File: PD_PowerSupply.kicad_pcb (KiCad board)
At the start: 2 copper layers, 77.1 x 77.1 mm, 12 parts, among them Q1 STL6P3LLH6, Q2 STL6P3LLH6, Q3 MMBT3906, Q4 MMBT3906, U1 STUSB4500QTR, U2 ESP32-WROOM-32, U3 CP2102N, U4 LTM8074IY#PBF, U5 LTM8074IY#PBF, U6 LTC2972

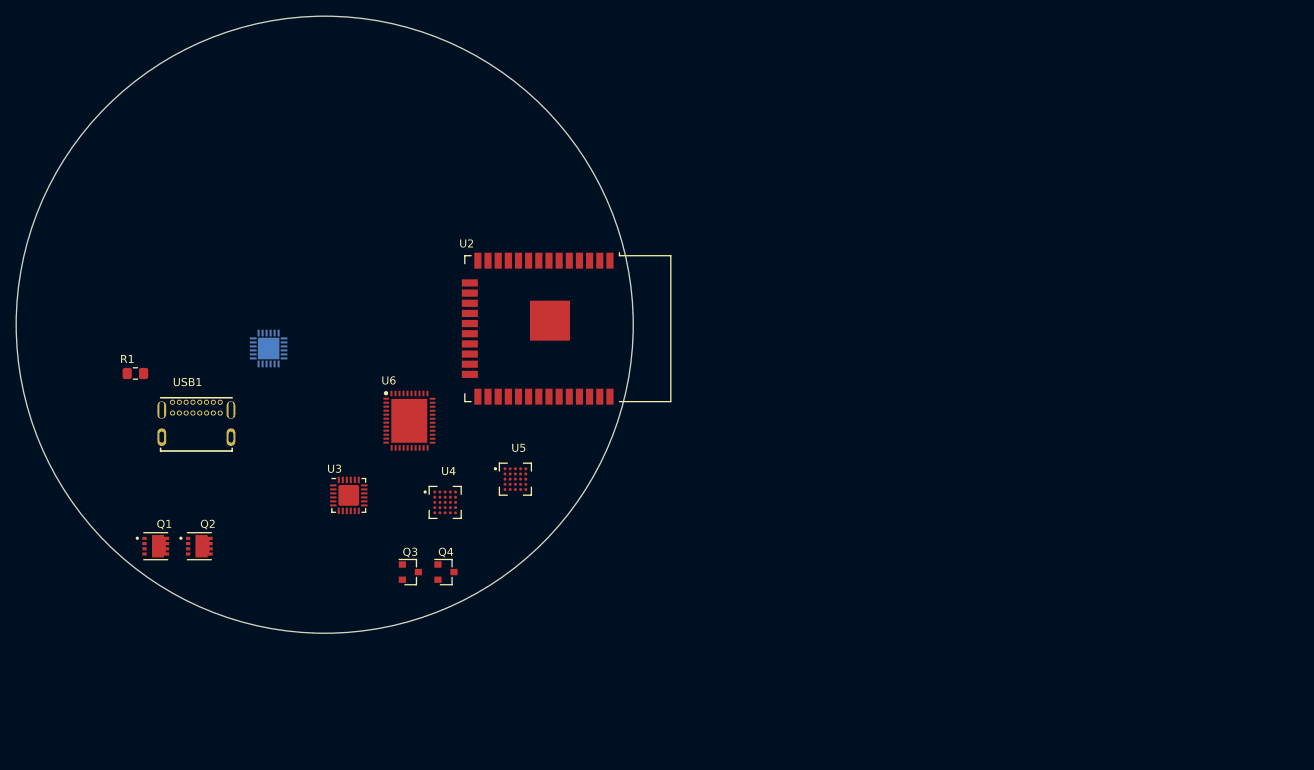
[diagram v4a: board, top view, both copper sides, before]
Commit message: integrated STM32 and assigned most footprints
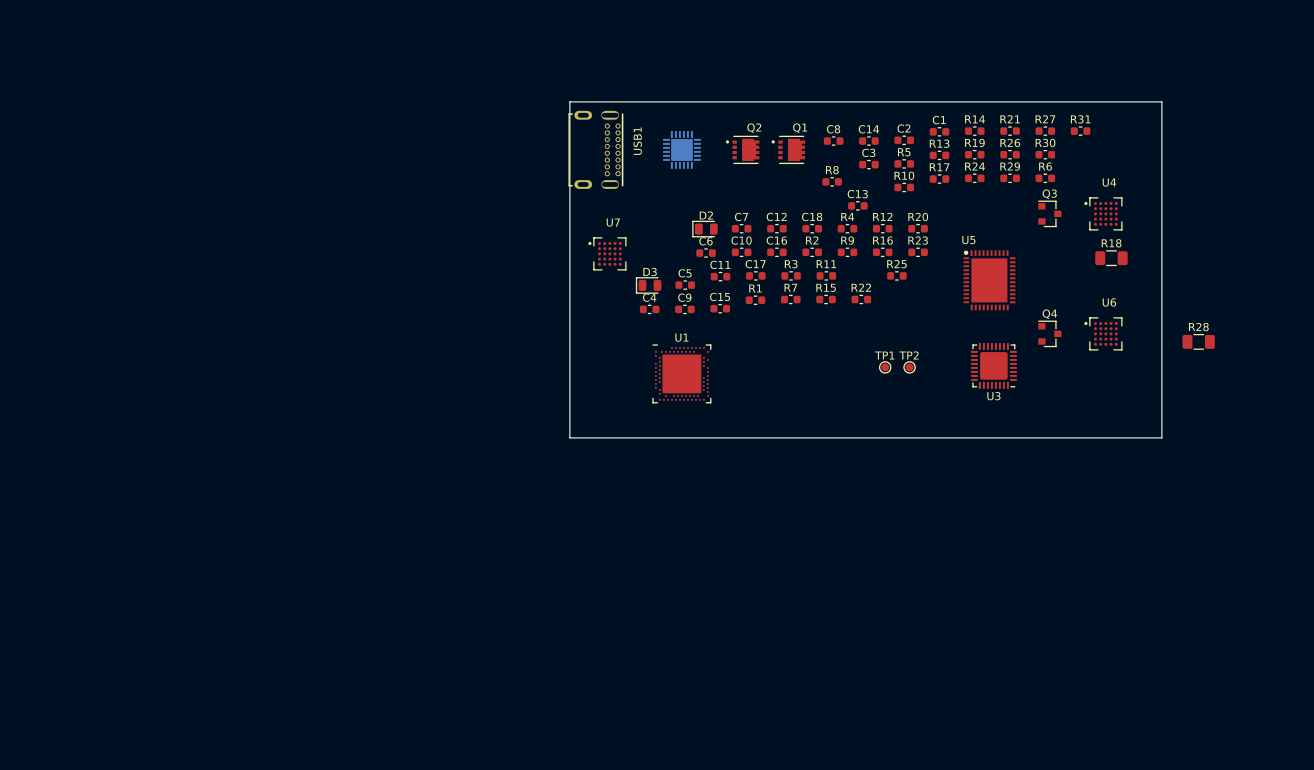
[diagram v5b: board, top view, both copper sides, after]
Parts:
- removed the U2 at (110.8, 102.3)
- removed the U5 at (107.2, 121.2)
- added C1: 1uF, Capacitor_SMD:C_0603_1608Metric, F.Cu at (160.2, 77.7)
- added C10: .01uF, Capacitor_SMD:C_0603_1608Metric, F.Cu at (135.5, 92.8)
- added C11: .1uF, Capacitor_SMD:C_0603_1608Metric, F.Cu at (132.8, 95.8)
- added C12: .1uF, Capacitor_SMD:C_0603_1608Metric, F.Cu at (139.9, 89.9)
- added C13: .1uF, Capacitor_SMD:C_0603_1608Metric, F.Cu at (150.0, 87.0)
- added C14: .1uF, Capacitor_SMD:C_0603_1608Metric, F.Cu at (151.4, 78.9)
- added C15: .1uF, Capacitor_SMD:C_0603_1608Metric, F.Cu at (132.8, 99.9)
- added C16: 1uF, Capacitor_SMD:C_0603_1608Metric, F.Cu at (139.9, 92.8)
- added C17: 10nF, Capacitor_SMD:C_0603_1608Metric, F.Cu at (137.2, 95.8)
- added C18: 10uF, Capacitor_SMD:C_0603_1608Metric, F.Cu at (144.3, 89.9)
- added C2: .1uF, Capacitor_SMD:C_0603_1608Metric, F.Cu at (155.8, 78.8)
- added C3: .1uF, Capacitor_SMD:C_0603_1608Metric, F.Cu at (151.4, 81.8)
- added C4: 1uF, Capacitor_SMD:C_0603_1608Metric, F.Cu at (124.0, 99.9)
- added C5: .1uF, Capacitor_SMD:C_0603_1608Metric, F.Cu at (128.4, 96.9)
- added C6: 10nF, Capacitor_SMD:C_0603_1608Metric, F.Cu at (131.0, 92.9)
- added C7: 1uF, Capacitor_SMD:C_0603_1608Metric, F.Cu at (135.5, 89.9)
- added C8: 1uF, Capacitor_SMD:C_0603_1608Metric, F.Cu at (147.0, 78.9)
- added C9: C, Capacitor_SMD:C_0603_1608Metric, F.Cu at (128.4, 99.9)
- added D2: GREEN 0805, LED_SMD:LED_0805_2012Metric, F.Cu at (131.1, 89.9)
- added D3: RED 0805, LED_SMD:LED_0805_2012Metric, F.Cu at (124.0, 96.9)
- added R10: 47.5k, Resistor_SMD:R_0603_1608Metric, F.Cu at (155.8, 84.7)
- added R11: 47.5k, Resistor_SMD:R_0603_1608Metric, F.Cu at (146.1, 95.8)
- added R12: 47.5k, Resistor_SMD:R_0603_1608Metric, F.Cu at (153.1, 89.9)
- added R13: 100, Resistor_SMD:R_0603_1608Metric, F.Cu at (160.2, 80.7)
- added R14: 300, Resistor_SMD:R_0603_1608Metric, F.Cu at (164.6, 77.7)
- added R15: 300, Resistor_SMD:R_0603_1608Metric, F.Cu at (146.0, 98.7)
- added R16: 1k, Resistor_SMD:R_0603_1608Metric, F.Cu at (153.1, 92.8)
- added R17: R_US, Resistor_SMD:R_0603_1608Metric, F.Cu at (160.2, 83.6)
- added R18: 20m, Resistor_SMD:R_1206_3216Metric, F.Cu at (181.7, 93.5)
- added R19: 10k, Resistor_SMD:R_0603_1608Metric, F.Cu at (164.6, 80.6)
- added R2: 470, Resistor_SMD:R_0603_1608Metric, F.Cu at (144.3, 92.8)
- added R20: R_Shunt_US, Resistor_SMD:R_0603_1608Metric, F.Cu at (157.5, 89.9)
- added R21: 10k, Resistor_SMD:R_0603_1608Metric, F.Cu at (169.0, 77.7)
- added R22: R_US, Resistor_SMD:R_0603_1608Metric, F.Cu at (150.4, 98.7)
- added R23: 10k, Resistor_SMD:R_0603_1608Metric, F.Cu at (157.5, 92.8)
- added R24: 10k, Resistor_SMD:R_0603_1608Metric, F.Cu at (164.6, 83.6)
- added R25: R_US, Resistor_SMD:R_0603_1608Metric, F.Cu at (154.9, 95.8)
- added R26: 10k, Resistor_SMD:R_0603_1608Metric, F.Cu at (169.0, 80.6)
- added R27: 10k, Resistor_SMD:R_0603_1608Metric, F.Cu at (173.4, 77.7)
- added R28: 20m, Resistor_SMD:R_1206_3216Metric, F.Cu at (192.6, 104.0)
- added R29: R_US, Resistor_SMD:R_0603_1608Metric, F.Cu at (169.0, 83.6)
- added R3: 1k, Resistor_SMD:R_0603_1608Metric, F.Cu at (141.7, 95.8)
- added R30: 23.7k, Resistor_SMD:R_0603_1608Metric, F.Cu at (173.4, 80.6)
- added R31: 76.8k, Resistor_SMD:R_0603_1608Metric, F.Cu at (177.8, 77.7)
- added R4: 100k, Resistor_SMD:R_0603_1608Metric, F.Cu at (148.7, 89.9)
- added R5: 100k, Resistor_SMD:R_0603_1608Metric, F.Cu at (155.8, 81.8)
- added R6: 47.5k, Resistor_SMD:R_0603_1608Metric, F.Cu at (173.4, 83.6)
- added R7: 10k, Resistor_SMD:R_0603_1608Metric, F.Cu at (141.6, 98.7)
- added R8: 22k, Resistor_SMD:R_0603_1608Metric, F.Cu at (146.8, 84.0)
- added R9: 100k, Resistor_SMD:R_0603_1608Metric, F.Cu at (148.7, 92.8)
- added TP1: TestPoint, TestPoint:TestPoint_Pad_D1.0mm, F.Cu at (153.4, 107.2)
- added TP2: TestPoint, TestPoint:TestPoint_Pad_D1.0mm, F.Cu at (156.5, 107.2)
- added U1: nRF52840, Package_DFN_QFN:Nordic_AQFN-73-1EP_7x7mm_P0.5mm, F.Cu at (128.0, 108.0)
- added U6: LTM8074IY#PBF, LTM8074IY_PBF:BGA25C65P5X5_400X400X198N, F.Cu at (181.0, 103.0)
- added U7: LTM8074IY#PBF, LTM8074IY_PBF:BGA25C65P5X5_400X400X198N, F.Cu at (119.0, 93.0)
- R1: value 22k -> 100k; footprint Resistor_SMD:R_0805_2012Metric_Pad1.15x1.40mm_HandSolder -> Resistor_SMD:R_0603_1608Metric
- U3: value CP2102N -> STM32L432KCUx; footprint Package_DFN_QFN:QFN-24-1EP_4x4mm_P0.5mm_EP2.6x2.6mm -> Package_DFN_QFN:QFN-32-1EP_5x5mm_P0.5mm_EP3.45x3.45mm
- moved Q1 93.7 mm to (141.7, 80.0)
- moved Q3 91.6 mm to (174.0, 88.0)
- moved U4 90.1 mm to (181.0, 88.0)
- moved Q2 84.4 mm to (136.0, 80.0)
- moved U3 82.2 mm to (167.0, 107.0), turned to 180 degrees
- moved Q4 81.1 mm to (174.0, 103.0)
- moved R1 78.0 mm to (137.2, 98.8)
- moved U5 74.6 mm to (166.5, 96.0)
- moved USB1 60.3 mm to (116.0, 80.0), turned to 270 degrees
- moved U2 57.3 mm to (128.0, 80.0)
- renumbered U1 to U2, U6 to U5
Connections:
- net Net-(D1-Pad2) renamed /VUSB_RAW
- net Net-(U3-Pad23) renamed /STM32_SWDIO
- net Net-(U3-Pad24) renamed /STM32_SWDCLK
- net Net-(U3-Pad7) renamed /SMBUS_ALERT
- R1 pad 1: Net-(Q1-Pad4) -> +3V3
- R1 pad 2: Net-(R1-Pad2) -> STUSB_ALERT
- U2 pad 16: Net-(R1-Pad2) -> Net-(R8-Pad2)
- U2 pad 19: /STUSB_ALERT -> STUSB_ALERT
- U3 pad 1: Net-(U3-Pad1) -> +3V3
- U3 pad 10: Net-(U3-Pad10) -> /FAULTB0
- U3 pad 11: Net-(U3-Pad11) -> /SPI_SCK
- U3 pad 12: Net-(U3-Pad12) -> /SPI_MISO
- U3 pad 13: Net-(U3-Pad13) -> /I2C_SCL
- U3 pad 16: Net-(U3-Pad16) -> GND
- U3 pad 17: Net-(U3-Pad17) -> +3V3
- U3 pad 19: Net-(U3-Pad19) -> /I2C_SCL_SMBUS
- U3 pad 2: GND -> Net-(U3-Pad2)
- U3 pad 20: Net-(U2-Pad35) -> /I2C_SDA_SMBUS
- U3 pad 21: Net-(U2-Pad34) -> /FAULTB1
- U3 pad 22: Net-(U3-Pad22) -> /SPI_MOSI
- U3 pad 25: GND -> Net-(D3-Pad2)
- U3 pad 3: /USB_DP -> Net-(U3-Pad3)
- U3 pad 4: /USB_DN -> Net-(R7-Pad2)
- U3 pad 6: +3V3 -> Net-(D2-Pad2)
- U3 pad 8: Net-(U3-Pad8) -> /CONTROL0
- U3 pad 9: Net-(U3-Pad9) -> /CONTROL1
- U4 pad E1: Net-(R13-Pad4) -> Net-(R18-Pad1)
- U4 pad E2: Net-(R13-Pad4) -> Net-(R18-Pad1)
- U5 pad 17: Net-(R14-Pad2) -> /FAULTB0
- U5 pad 18: Net-(R22-Pad2) (its old number) -> /FAULTB1
- U5 pad 20: Net-(U6-Pad20) -> /I2C_SDA_SMBUS
- U5 pad 21: Net-(U6-Pad21) -> /I2C_SCL_SMBUS
- U5 pad 23: Net-(R18-Pad2) -> /CONTROL0
- U5 pad 24: Net-(R19-Pad2) -> /CONTROL1
- U5 pad 30: Net-(R13-Pad3) -> Net-(R18-Pad1)
- U5 pad 31: Net-(R13-Pad2) -> Net-(J1-Pad1)
- U5 pad 35: Net-(R23-Pad2) -> Net-(J2-Pad1)
- U5 pad 45: (no net) -> GND
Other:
- board size 77.1 x 77.1 mm -> 74 x 42 mm

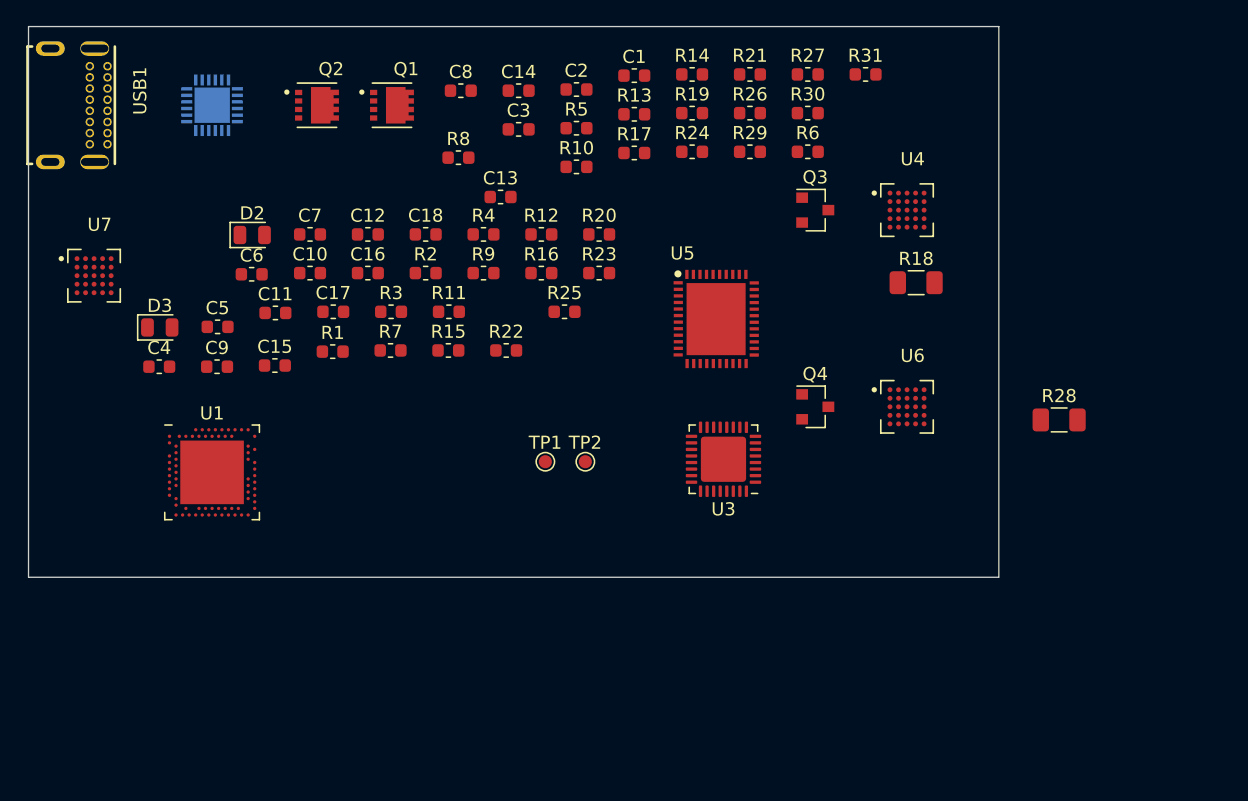
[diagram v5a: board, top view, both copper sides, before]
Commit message: added debug and power out connectors
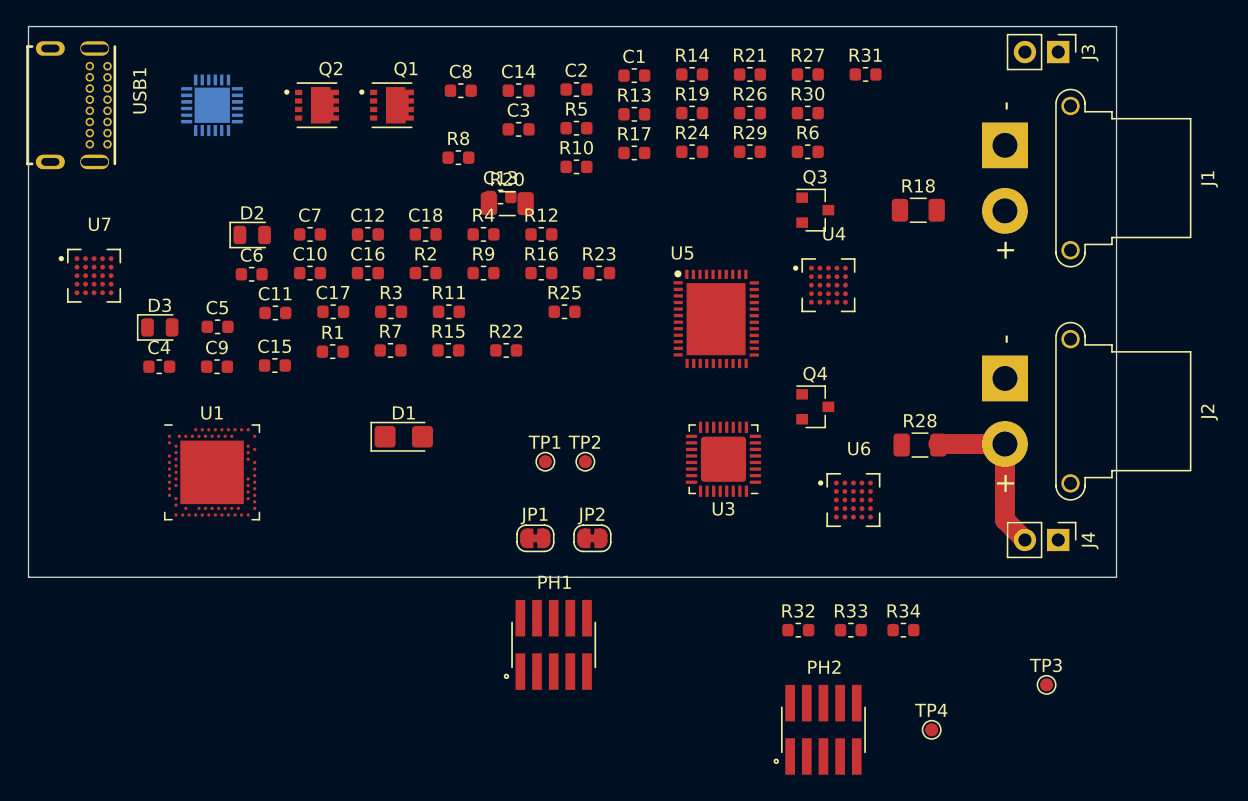
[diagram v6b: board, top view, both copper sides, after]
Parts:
- added D1: D_Schottky, Diode_SMD:D_1206_3216Metric_Castellated, F.Cu at (142.6, 105.3)
- added J1: Connector, Connector_AMASS:AMASS_XT30PW-F_1x02_P2.50mm_Horizontal, F.Cu at (188.5, 83.1)
- added J2: Connector, Connector_AMASS:AMASS_XT30PW-F_1x02_P2.50mm_Horizontal, F.Cu at (188.5, 100.8)
- added J3: Connector, Connector_PinHeader_2.54mm:PinHeader_1x02_P2.54mm_Vertical, F.Cu at (192.5, 75.9)
- added J4: Connector, Connector_PinHeader_2.54mm:PinHeader_1x02_P2.54mm_Vertical, F.Cu at (192.5, 113.2)
- added JP1: SolderJumper_2_Bridged, Jumper:SolderJumper-2_P1.3mm_Bridged_RoundedPad1.0x1.5mm, F.Cu at (152.7, 113.0)
- added JP2: SolderJumper_2_Bridged, Jumper:SolderJumper-2_P1.3mm_Bridged_RoundedPad1.0x1.5mm, F.Cu at (157.0, 113.0)
- added PH1: FTSH-105-01-L-DV-K, FTSH-105-01-L-DV-K:SAMTEC_FTSH-105-01-L-DV-K, F.Cu at (154.1, 121.2)
- added PH2: FTSH-105-01-L-DV-K, FTSH-105-01-L-DV-K:SAMTEC_FTSH-105-01-L-DV-K, F.Cu at (174.6, 127.6)
- added R32: 40.2k, Resistor_SMD:R_0603_1608Metric, F.Cu at (172.7, 120.0)
- added R33: 40.2k, Resistor_SMD:R_0603_1608Metric, F.Cu at (176.7, 120.0)
- added R34: 10k, Resistor_SMD:R_0603_1608Metric, F.Cu at (180.7, 120.0)
- added TP3: TestPoint, TestPoint:TestPoint_Pad_D1.0mm, F.Cu at (191.6, 124.2)
- added TP4: TestPoint, TestPoint:TestPoint_Pad_D1.0mm, F.Cu at (182.9, 127.6)
- R20: value R_Shunt_US -> 20m; footprint Resistor_SMD:R_0603_1608Metric -> Resistor_SMD:R_1206_3216Metric
- moved R28 10.8 mm to (182.0, 105.9)
- moved U4 8.29 mm to (175.0, 93.7)
- moved U6 8.20 mm to (176.9, 110.1)
- moved R20 7.39 mm to (150.5, 87.5)
- moved R18 5.53 mm to (181.9, 88.0)
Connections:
- net Net-(R7-Pad2) renamed /STM32_NRST
- R1 pad 2: STUSB_ALERT -> /STUSB_ALERT
- R20 pad 2: Net-(R20-Pad2) -> VBUS
- U1 pad AA24: Net-(DBG1-Pad4) -> /NRF_SWDCLK
- U1 pad AC13: Net-(DBG1-Pad10) -> /NRF_NRST
- U1 pad AC24: Net-(DBG1-Pad2) -> /NRF_SWDIO
- U2 pad 19: STUSB_ALERT -> /STUSB_ALERT
- U3 pad 18: Net-(U3-Pad18) -> /STUSB_ALERT
- U3 pad 26: Net-(U3-Pad26) -> /STM32_SWO
- U4 pad D5: Net-(U4-PadD5) -> GND
- U5 pad 43: Net-(R20-Pad2) -> /vSINK
- U5 pad 44: Net-(R20-Pad3) -> VBUS
- U6 pad D5: Net-(U6-PadD5) -> GND
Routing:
- net Net-(J2-Pad2): track 0.00 -> 13.1 mm
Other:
- board size 74 x 42 mm -> 83 x 42 mm
